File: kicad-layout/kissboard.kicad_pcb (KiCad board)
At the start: 2 copper layers, 131.1 x 102.7 mm, 27 parts, among them J1 Conn_01x04, K1 KEYSW, K10 KEYSW, K11 KEYSW, K12 KEYSW, K13 KEYSW, K14 KEYSW, K15 KEYSW, K16 KEYSW, K17 KEYSW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

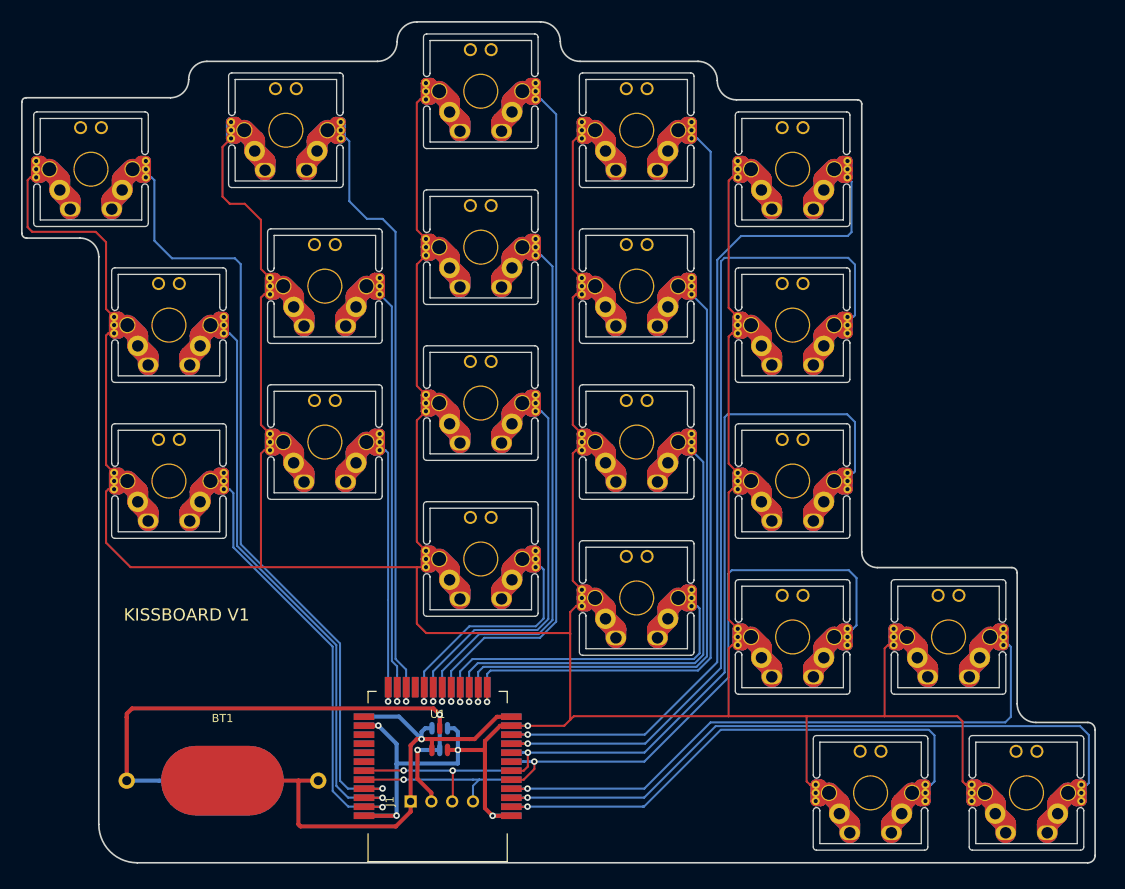
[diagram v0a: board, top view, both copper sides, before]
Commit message: Adjusted edge cut, updated pictures and pdf prints
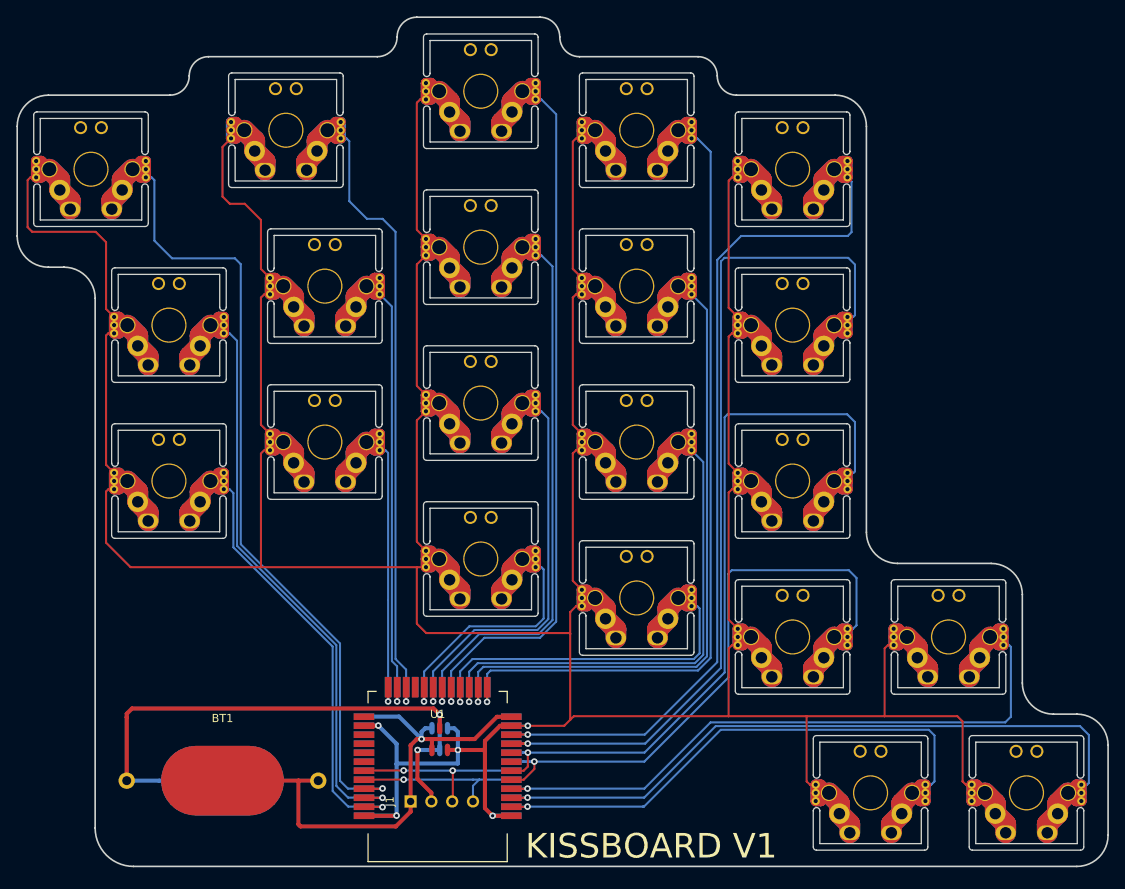
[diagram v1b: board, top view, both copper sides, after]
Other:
- board size 131.1 x 102.7 mm -> 133.3 x 103.8 mm
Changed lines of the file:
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@@
       (net 16 GND))
   )
-  (gr_text "KISSBOARD V1" (at 54.61 94.9325) (layer B.SilkS)
-    (effects (font (size 1.5 1.5) (thickness 0.3)) (justify mirror))
+  (gr_arc (start 163.321471 121.8565) (end 163.321471 125.667029) (angle -90) (layer Edge.Cuts) (width 0.2))
+  (gr_arc (start 163.322 110.871529) (end 167.132529 110.871529) (angle -90) (layer Edge.Cuts) (width 0.2))
+  (gr_arc (start 160.465029 103.251) (end 156.6545 103.251) (angle -90) (layer Edge.Cuts) (width 0.2))
+  (gr_arc (start 152.8445 92.456529) (end 156.655029 92.456529) (angle -90) (layer Edge.Cuts) (width 0.2))
+  (gr_arc (start 141.4145 84.835471) (end 137.603971 84.835471) (angle -90) (layer Edge.Cuts) (width 0.2))
+  (gr_arc (start 133.7945 35.243029) (end 137.605029 35.243029) (angle -90) (layer Edge.Cuts) (width 0.2))
+  (gr_arc (start 37.656029 35.2425) (end 37.656029 31.431971) (angle -90) (layer Edge.Cuts) (width 0.2))
+  (gr_line (start 52.5145 31.4325) (end 37.6555 31.4325) (layer Edge.Cuts) (width 0.2))
+  (gr_arc (start 57.213142 29.083) (end 57.213142 26.7335) (angle -90) (layer Edge.Cuts) (width 0.2))
+  (gr_arc (start 52.514142 29.083) (end 52.514142 31.4325) (angle -90) (layer Edge.Cuts) (width 0.2))
+  (gr_line (start 37.6555 52.451) (end 39.5605 52.451) (layer Edge.Cuts) (width 0.2))
+  (gr_arc (start 39.5605 56.261529) (end 43.371029 56.261529) (angle -90) (layer Edge.Cuts) (width 0.2))
+  (gr_arc (start 37.656029 48.641) (end 33.8455 48.641) (angle -90) (layer Edge.Cuts) (width 0.2))
+  (gr_text "KISSBOARD V1" (at 111.379 123.19) (layer B.SilkS)
+    (effects (font (size 3 3) (thickness 0.3)) (justify mirror))
   )
-  (gr_text "KISSBOARD V1" (at 54.5465 94.9325) (layer F.SilkS)
-    (effects (font (size 1.5 1.5) (thickness 0.3)))
+  (gr_text "KISSBOARD V1" (at 111.3155 123.19) (layer F.SilkS)
+    (effects (font (size 3 3) (thickness 0.3)))
   )
-  (gr_arc (start 34.9885 48.3235) (end 34.417 48.3235) (angle -90) (layer Edge.Cuts) (width 0.2))
-  (gr_line (start 34.417 48.3235) (end 34.417 32.258) (layer Edge.Cuts) (width 0.2))
-  (gr_arc (start 52.578 29.5275) (end 52.578 31.75) (angle -90) (layer Edge.Cuts) (width 0.2))
-  (gr_arc (start 57.023 29.5275) (end 57.023 27.305) (angle -90) (layer Edge.Cuts) (width 0.2))
-  (gr_arc (start 155.3845 89.789) (end 156.0195 89.789) (angle -90) (layer Edge.Cuts) (width 0.2))
-  (gr_arc (start 121.7295 29.6545) (end 119.38 29.6545) (angle -90) (layer Edge.Cuts) (width 0.2))
-  (gr_arc (start 117.0305 29.6545) (end 119.38 29.6545) (angle -90) (layer Edge.Cuts) (width 0.2))
-  (gr_arc (start 102.616 24.892) (end 100.203 24.892) (angle -90) (layer Edge.Cuts) (width 0.2))
-  (gr_arc (start 97.79 24.892) (end 100.203 24.892) (angle -90) (layer Edge.Cuts) (width 0.2))
-  (gr_arc (start 34.925 32.257976) (end 34.925 31.749976) (angle -90) (layer Edge.Cuts) (width 0.2))
-  (gr_arc (start 77.851 24.892) (end 77.851 27.305) (angle -90) (layer Edge.Cuts) (width 0.2))
-  (gr_arc (start 82.677 24.892) (end 82.677 22.479) (angle -90) (layer Edge.Cuts) (width 0.2))
-  (gr_arc (start 136.525 32.512) (end 137.033 32.512) (angle -90) (layer Edge.Cuts) (width 0.2))
-  (gr_arc (start 138.938 87.249) (end 137.033 87.249) (angle -90) (layer Edge.Cuts) (width 0.2))
-  (gr_arc (start 158.3055 105.791) (end 156.0195 105.791) (angle -90) (layer Edge.Cuts) (width 0.2))
-  (gr_arc (start 41.529 51.181) (end 43.815 51.181) (angle -90) (layer Edge.Cuts) (width 0.2))
-  (gr_arc (start 48.514 120.523) (end 48.514 125.222) (angle 90) (layer Edge.Cuts) (width 0.2))
-  (gr_arc (start 164.6555 124.333) (end 164.6555 125.222) (angle -90) (layer Edge.Cuts) (width 0.2))
-  (gr_arc (start 164.6555 108.966) (end 165.5445 108.966) (angle -90) (layer Edge.Cuts) (width 0.2))
-  (gr_line (start 117.0305 27.305) (end 102.616 27.305) (layer Edge.Cuts) (width 0.2))
-  (gr_line (start 136.525 32.004) (end 121.729361 32.004) (layer Edge.Cuts) (width 0.2))
-  (gr_line (start 137.033 87.249) (end 137.033 32.512) (layer Edge.Cuts) (width 0.2))
-  (gr_line (start 155.3845 89.154) (end 138.938 89.154) (layer Edge.Cuts) (width 0.2))
-  (gr_line (start 156.0195 105.791) (end 156.0195 89.789) (layer Edge.Cuts) (width 0.2))
-  (gr_line (start 164.655817 108.077) (end 158.3055 108.077) (layer Edge.Cuts) (width 0.2))
-  (gr_line (start 165.5445 124.333) (end 165.5445 108.966) (layer Edge.Cuts) (width 0.2))
-  (gr_line (start 48.514 125.222) (end 164.6555 125.222) (layer Edge.Cuts) (width 0.2))
-  (gr_line (start 43.815 51.181) (end 43.815 120.523) (layer Edge.Cuts) (width 0.2))
-  (gr_line (start 34.9885 48.895) (end 41.529 48.895) (layer Edge.Cuts) (width 0.2))
-  (gr_line (start 52.578 31.75) (end 34.925 31.75) (layer Edge.Cuts) (width 0.2))
-  (gr_line (start 77.851358 27.305) (end 57.023 27.305) (layer Edge.Cuts) (width 0.2))
-  (gr_line (start 97.79 22.479) (end 82.677 22.479) (layer Edge.Cuts) (width 0.2))
+  (gr_line (start 33.8455 48.641) (end 33.8455 35.2425) (layer Edge.Cuts) (width 0.2))
+  (gr_arc (start 121.7295 29.083) (end 119.38 29.083) (angle -90) (layer Edge.Cuts) (width 0.2))
+  (gr_arc (start 117.0305 29.083) (end 119.38 29.083) (angle -90) (layer Edge.Cuts) (width 0.2))
+  (gr_arc (start 102.5525 24.3205) (end 100.1395 24.3205) (angle -90) (layer Edge.Cuts) (width 0.2))
+  (gr_arc (start 97.7265 24.3205) (end 100.1395 24.3205) (angle -90) (layer Edge.Cuts) (width 0.2))
+  (gr_arc (start 77.851 24.3205) (end 77.851 26.7335) (angle -90) (layer Edge.Cuts) (width 0.2))
+  (gr_arc (start 82.677 24.3205) (end 82.677 21.9075) (angle -90) (layer Edge.Cuts) (width 0.2))
+  (gr_arc (start 48.0695 120.9675) (end 48.0695 125.6665) (angle 90) (layer Edge.Cuts) (width 0.2))
+  (gr_line (start 117.0305 26.7335) (end 102.5525 26.7335) (layer Edge.Cuts) (width 0.2))
+  (gr_line (start 133.794667 31.4325) (end 121.729369 31.4325) (layer Edge.Cuts) (width 0.2))
+  (gr_line (start 137.6045 84.836162) (end 137.6045 35.2425) (layer Edge.Cuts) (width 0.2))
+  (gr_line (start 152.8445 88.646) (end 141.4145 88.646) (layer Edge.Cuts) (width 0.2))
+  (gr_line (start 156.6545 103.251) (end 156.6545 92.456) (layer Edge.Cuts) (width 0.2))
+  (gr_line (start 163.322705 107.061) (end 160.4645 107.061) (layer Edge.Cuts) (width 0.2))
+  (gr_line (start 167.132 121.8565) (end 167.132 110.870421) (layer Edge.Cuts) (width 0.2))
+  (gr_line (start 48.0695 125.6665) (end 163.322 125.6665) (layer Edge.Cuts) (width 0.2))
+  (gr_line (start 43.3705 56.261) (end 43.3705 120.9675) (layer Edge.Cuts) (width 0.2))
+  (gr_line (start 77.851 26.7335) (end 57.213403 26.7335) (layer Edge.Cuts) (width 0.2))
+  (gr_line (start 97.7265 21.9075) (end 82.677 21.9075) (layer Edge.Cuts) (width 0.2))
   (segment (start 86.87054 105.5243) (end 86.87054 103.78454) (width 0.25) (layer F.Cu) (net 4))
   (segment (start 86.87054 103.78454) (end 86.867 103.781) (width 0.25) (layer F.Cu) (net 4))
